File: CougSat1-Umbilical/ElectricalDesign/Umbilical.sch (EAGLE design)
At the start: 5 parts, among them J2 HR10A-10P-10P, J3 EJ501C

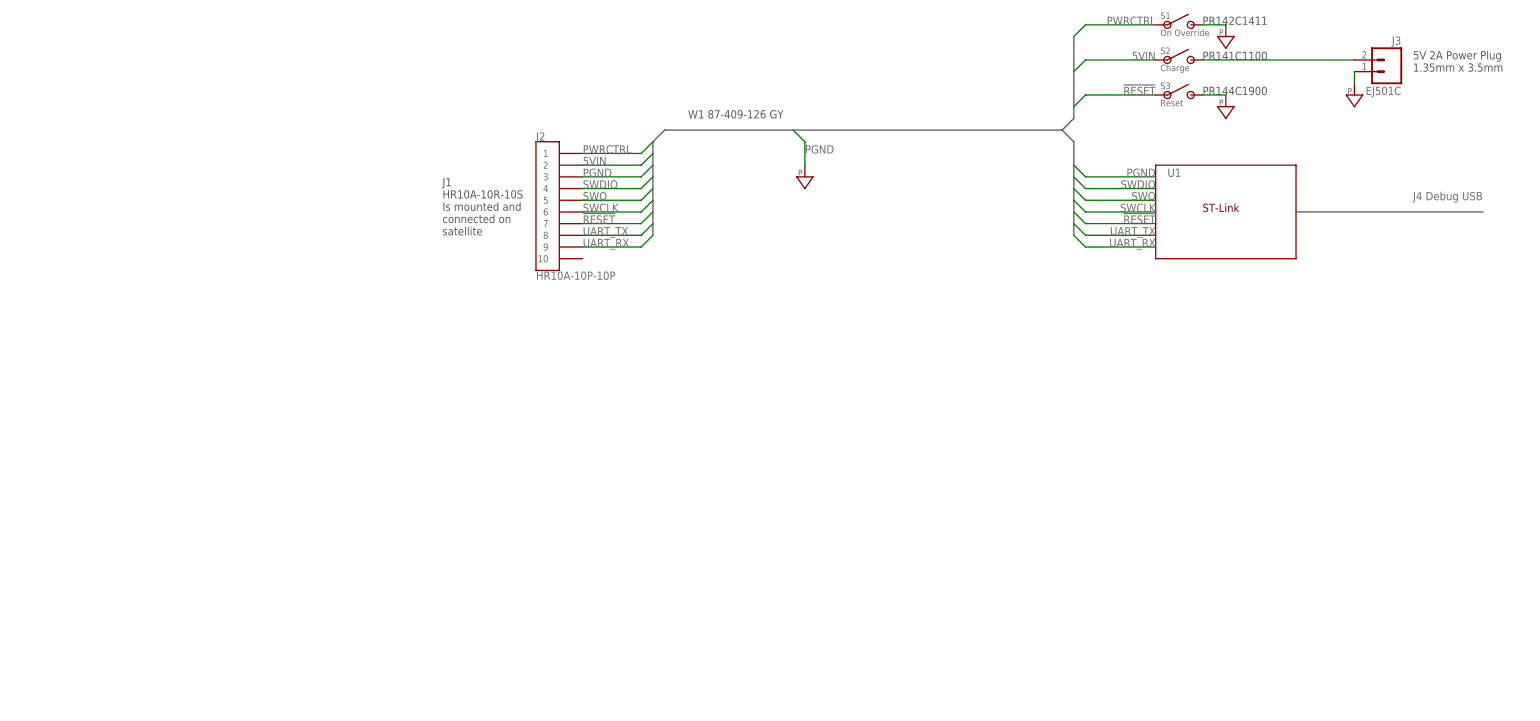
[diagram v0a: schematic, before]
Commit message: Created Umbilical Block Diagram
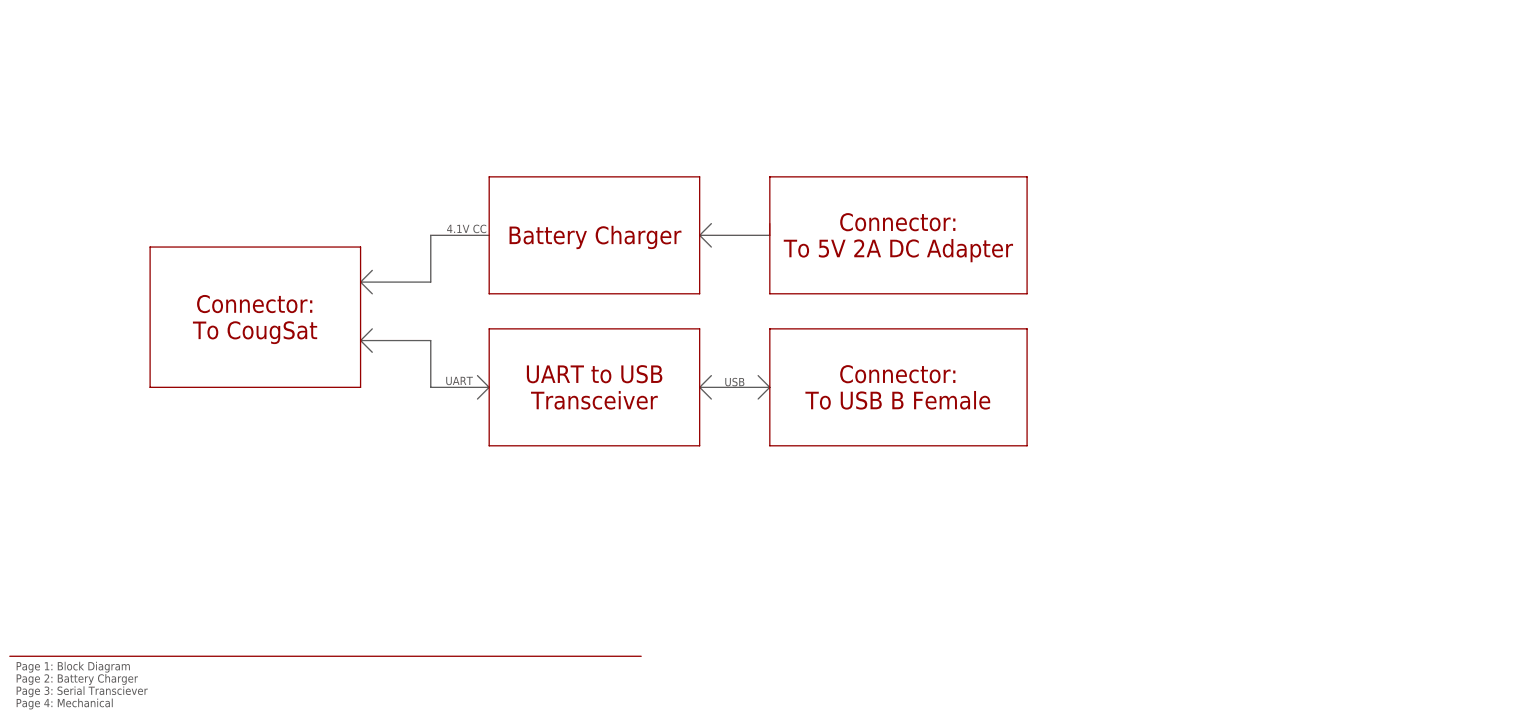
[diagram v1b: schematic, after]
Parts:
- removed J2: HR10A-10P-10P, CougsInSpace:CONN_101X10_SMD-2.5MM
- removed J3: EJ501C, CougsInSpace:CONN_021X02_SMD-2.5MM
- removed S1: On Override, CougsInSpace:TACTILE_SWITCH6.2MMX6.2MM
- removed S2: Charge, CougsInSpace:TACTILE_SWITCH6.2MMX6.2MM
- removed S3: Reset, CougsInSpace:TACTILE_SWITCH6.2MMX6.2MM
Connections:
- removed net !RESET: J2.7, S3.1
- removed net 5VIN: J2.2, S2.1
- removed net N$1: J3.2, S2.2
- removed net PGND: J2.3, J3.1, S1.2, S3.2
- removed net PWRCTRL: J2.1, S1.1
- removed net SWCLK: J2.6
- removed net SWDIO: J2.4
- removed net SWO: J2.5
- removed net UART_RX: J2.9
- removed net UART_TX: J2.8
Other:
- note added: "4.1V CC"
- note added: "Battery Charger"
- note added: "Connector: To 5V 2A DC Adapter"
- note added: "Connector: To CougSat"
- note added: "Connector: To USB B Female"
- note added: "Page 1: Block Diagram Page 2: Battery Charger Page 3: Serial Transciever Page 4: Mechanical"
- note added: "UART"
- note added: "UART to USB Transceiver"
- note added: "USB"
- note removed: "5V 2A Power Plug 1.35mm x 3.5mm"
- note removed: "J1 HR10A-10R-10S Is mounted and connected on satellite"
- note removed: "J4 Debug USB"
- note removed: "PR141C1100"
- note removed: "PR142C1411"
- note removed: "PR144C1900"
- note removed: "ST-Link"
- note removed: "U1"
- note removed: "W1 87-409-126 GY"

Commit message: Update CougSat1-Umbilical/ElectricalDesign/Umbilical.sch
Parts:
- added C1, C10, C12, C4: 100nF 10%, CougsInSpace-Capacitors:CAP-V-100NF-1608
- added C11, C7, C8: 1µF 10%, CougsInSpace-Capacitors:CAP-V-1UF-1608
- added C13, C9: 10µF 10%, CougsInSpace-Capacitors:CAP-V-10UF-1608
- added C14: 4.7µF 10%, CougsInSpace-Capacitors:CAP-V-4.7UF-3216
- added C15: 22pF 5%, CougsInSpace-Capacitors:CAP-V-22PF-1608
- added C2, C3: 47pF 5%, CougsInSpace-Capacitors:CAP-V-47PF-1608
- added C5: 10nF 10%, CougsInSpace-Capacitors:CAP-V-10NF-1608
- added C6: 4.7pF ±0.1, CougsInSpace-Capacitors:CAP-V-4.7PF-1608
- added D1: LTC4411, CougsInSpace-DiscreteSemi:LTC4411
- added D2: MBRM120LT, CougsInSpace-DiscreteSemi:DIODE-SCHOTTKY-H-POWERMITE
- added DS1: Green, CougsInSpace-LEDs:LED-H-GRN-1608
- added DS2: Red, CougsInSpace-LEDs:LED-H-RED-1608
- added FB1: 1.5kΩ @ 100MHz, CougsInSpace-Coils:CHOKE-H-1.5K-1608
- added J1: (no value), CougsInSpace-Connectors:USB-B-FEMALE
- added J2: (no value), CougsInSpace-Connectors:1X04-PICOLOCK
- added J3: (no value), CougsInSpace-Connectors:BARREL-2.1X5.5-R
- added L1: 10µH 20%, CougsInSpace-Coils:INDUCTOR-H-10UH-6060
- added Q1, Q2: CSD16406Q3, CougsInSpace-DiscreteSemi:MOSFET-N-SON-3333
- added R1: 0Ω <20mΩ, CougsInSpace-Resistors:RES-V-0-1608
- added R10: 12.1kΩ 0.1%, CougsInSpace-Resistors:RES-V-12.1K-1608
- added R11: 2.2kΩ 1%, CougsInSpace-Resistors:RES-V-2.2K-1608
- added R12: 3.3kΩ 0.1%, CougsInSpace-Resistors:RES-V-3.3K-1608
- added R2, R3: 27Ω 1%, CougsInSpace-Resistors:RES-H-27R-1608
- added R4: 10Ω 5%, CougsInSpace-Resistors:RES-H-10R-TO220
- added R5, R6: 10kΩ 0.1%, CougsInSpace-Resistors:RES-H-10K-1608
- added R7: 10mΩ 1%, CougsInSpace-Resistors:RES-H-0.01R-3216
- added R8: 10mΩ 1%, CougsInSpace-Resistors:RES-V-0.01R-3216
- added R9: 10kΩ 0.1%, CougsInSpace-Resistors:RES-V-10K-1608
- added U1: FT230XQ, CougsInSpace-IC-Conversion:FT230X-QFN16
- added U2: BQ24650, CougsInSpace-IC-Power:BQ24650
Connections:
- new net 3.3V: C1.1, U1.!RESET, U1.3V3OUT, U1.VCCIO
- new net 5.0V: D1.IN, J3.CENTER, R5.1, R6.1, U2.MPPSET
- new net DGND: C1.2, R1.1, U1.DGND
- new net N$1: C11.1, D2.A, U2.REGN
- new net N$10: C8.1, R11.2, U2.VREF
- new net N$11: C10.2, L1.1, Q1.D, Q2.S, U2.PH
- new net N$12: Q2.G, U2.HIGHDV
- new net N$13: Q1.G, U2.LODRV
- new net N$14: R7.2, R8.2
- new net N$15: C12.1, L1.2, R7.1, U2.SR_P
- new net N$16: C12.2, C13.1, C14.1, C15.1, R8.1, R9.2, U2.SR_N
- new net N$18: C15.2, R10.2, R9.1, U2.VFB
- new net N$19: R11.1, R12.2, U2.TS
- new net N$2: C9.1, D1.OUT, Q2.D, R4.1
- new net N$3: U2.THERM_EN
- new net N$4: C10.1, D2.C, U2.BTST
- new net N$5: DS1.C, U2.STAT2
- new net N$6: C7.1, R4.2, U2.VCC
- new net N$7: DS1.A, R5.2
- new net N$8: DS2.A, R6.2
- new net N$9: DS2.C, U2.STAT1
- new net PGND: C11.2, C13.2, C14.2, C2.2, C3.2, C4.2, C5.2, C6.2, C7.2, C8.2, C9.2, D1.CTL, D1.GND, D1.STAT, J1.GND, J1.SHIELD, J2.4, J3.SLEEVE, J3.SW, Q1.S, R1.2, R10.1, R12.1, U2.PAD, U2.PGND
- new net UMB_IN: J2.1
- new net UMB_RX: J2.2, U1.TXD
- new net UMB_TX: J2.3, U1.RXD
- new net USB5V: C5.1, FB1.1, J1.VCC
- new net USB5V_FILTERED: C4.1, C6.1, FB1.2, U1.VCC
- new net USB_CONN_N: C2.1, J1.DATA_N, R3.1
- new net USB_CONN_P: C3.1, J1.DATA_P, R2.1
- new net USB_N: R3.2, U1.USBD_N
- new net USB_P: R2.2, U1.USBD_P
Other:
- note added: "2xx>"
- note added: "3XX>"
- note added: "CAD Note: Decoupling"

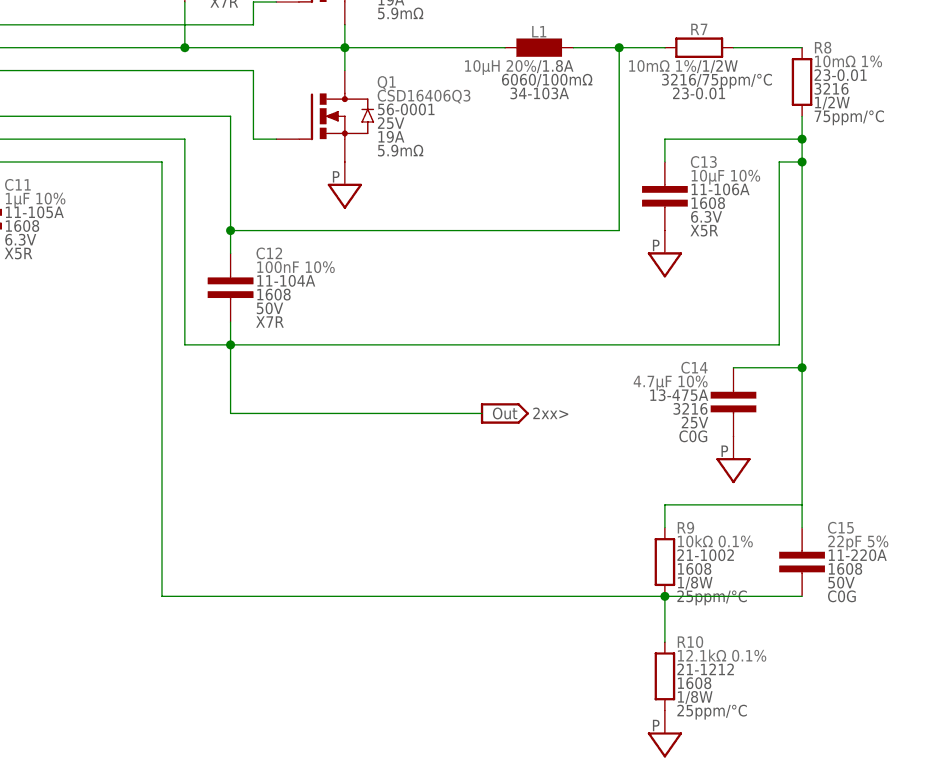
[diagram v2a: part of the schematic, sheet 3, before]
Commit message: Update CougSat1-Umbilical/ElectricalDesign/Umbilical.sch
Finished Umbilical schematic
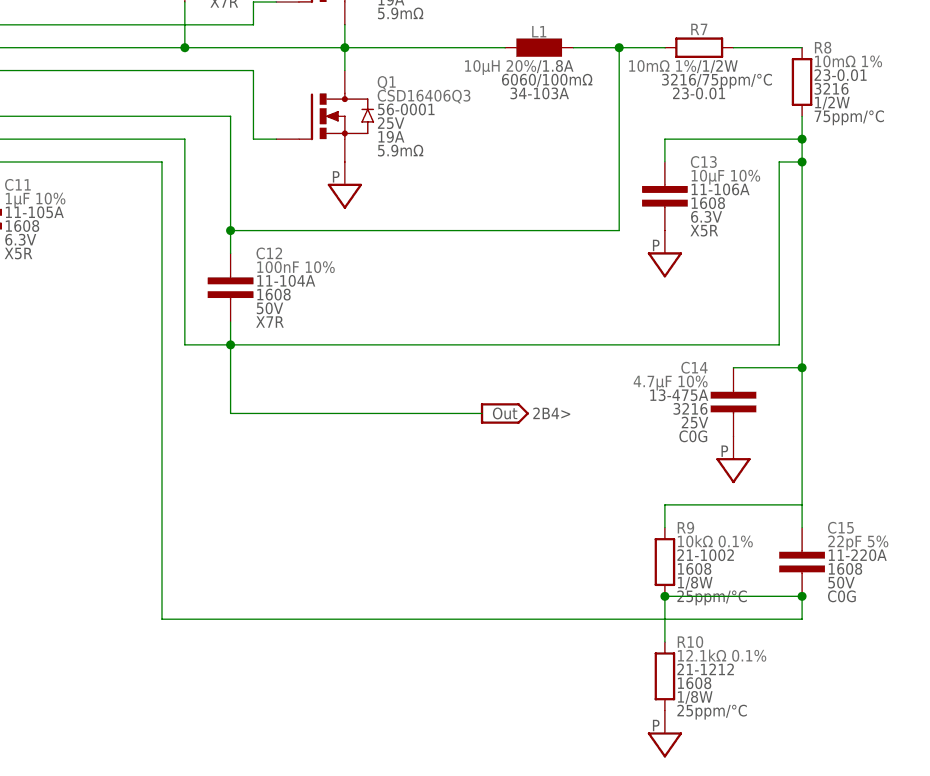
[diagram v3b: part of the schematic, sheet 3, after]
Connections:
- net N$1 renamed REGN
- net N$10 renamed VREF
- net N$11 renamed PH
- net N$12 renamed HIGHDV
- net N$13 renamed LODRV
- net N$15 renamed SR_P
- net N$16 renamed BAT_CHARGE_OUT
- net N$18 renamed VFB
- net N$19 renamed TS
- net N$2 renamed DIODE_OUT
- net N$4 renamed BTST
- net N$5 renamed CHARGING_STAT_G
- net N$6 renamed VCC
- net N$9 renamed CHARGING_STAT_R
- new net BARREL_MPPSET: D1.IN, J3.CENTER, U2.MPPSET
- net 5.0V: no longer D1.IN, J3.CENTER, U2.MPPSET
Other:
- note added: "2B4>"
- note added: "3C5>"
- note added: "Page 2"
- note added: "Page 3"
- note removed: "2xx>"
- note removed: "3XX>"
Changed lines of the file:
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@@
 <attribute name="TITLE" value="Block Diagram"/>
 </part>
-<part name="FRAME2" library="CougsInSpace-Aesthetics" deviceset="FRAME-A" device=""/>
+<part name="FRAME2" library="CougsInSpace-Aesthetics" deviceset="FRAME-A" device="">
+<attribute name="TITLE" value="Serial Transeiver"/>
+</part>
 <part name="U1" library="CougsInSpace-IC-Conversion" deviceset="FT230X" device="-QFN16" value="FT230XQ"/>
 <part name="J1" library="CougsInSpace-Connectors" deviceset="USB" device="-B-FEMALE"/>
@@
 <part name="C5" library="CougsInSpace-Capacitors" deviceset="CAP-V" device="-1608" technology="-10NF" value="10nF 10%"/>
 <part name="C6" library="CougsInSpace-Capacitors" deviceset="CAP-V" device="-1608" technology="-4.7PF" value="4.7pF ±0.1"/>
-<part name="FRAME3" library="CougsInSpace-Aesthetics" deviceset="FRAME-A" device=""/>
+<part name="FRAME3" library="CougsInSpace-Aesthetics" deviceset="FRAME-A" device="">
+<attribute name="TITLE" value="Battery Charger"/>
+</part>
 <part name="U2" library="CougsInSpace-IC-Power" deviceset="BQ24650" device="" value="BQ24650"/>
 <part name="C7" library="CougsInSpace-Capacitors" deviceset="CAP-V" device="-1608" technology="-1UF" value="1µF 10%"/>
@@
 <text x="100.584" y="84.328" size="1.778" layer="97" align="bottom-right">UART</text>
 <text x="157.48" y="84.074" size="1.778" layer="97" align="bottom-center">USB</text>
+<text x="147.32" y="73.66" size="1.27" layer="97" rot="R180" align="center-left">Page 2</text>
+<text x="147.32" y="106.68" size="1.27" layer="97" rot="R180" align="center-left">Page 3</text>
 </plain>
 <instances>
@@
 <wire x1="101.6" y1="101.6" x2="132.08" y2="101.6" width="0.1524" layer="97" style="shortdash"/>
 <text x="104.14" y="76.2" size="1.778" layer="97">CAD Note: Decoupling</text>
-<text x="137.16" y="134.62" size="1.27" layer="97" align="center-right">3XX&gt; </text>
+<text x="137.16" y="134.62" size="1.27" layer="97" align="center-right">3C5&gt; </text>
 </plain>
 <instances>
@@
 <attribute name="REV" x="257.81" y="7.62" size="3.81" layer="94" ratio="15" align="bottom-right"/>
 <attribute name="SHEET" x="257.81" y="1.27" size="3.81" layer="94" ratio="15" align="bottom-right"/>
+<attribute name="TITLE" x="227.33" y="20.32" size="3.81" layer="94" ratio="15" align="bottom-right"/>
 </instance>
 <instance part="U1" gate="G$1" x="116.84" y="121.92" smashed="yes">
@@
 <sheet>
 <plain>
-<text x="215.9" y="68.58" size="1.27" layer="97" align="center-left"> 2xx&gt;</text>
+<text x="215.9" y="68.58" size="1.27" layer="97" align="center-left"> 2B4&gt;</text>
 </plain>
 <instances>
@@
 <attribute name="REV" x="257.81" y="7.62" size="3.81" layer="94" ratio="15" align="bottom-right"/>
 <attribute name="SHEET" x="257.81" y="1.27" size="3.81" layer="94" ratio="15" align="bottom-right"/>
+<attribute name="TITLE" x="227.33" y="20.32" size="3.81" layer="94" ratio="15" align="bottom-right"/>
 </instance>
 <instance part="U2" gate="G$1" x="132.08" y="111.76" smashed="yes">
@@
 </segment>
 </net>
-<net name="N$2" class="0">
+<net name="DIODE_OUT" class="0">
 <segment>
 <pinref part="R4" gate="G$1" pin="1"/>
@@
 </segment>
 </net>
-<net name="N$4" class="0">
+<net name="BTST" class="0">
 <segment>
 <pinref part="U2" gate="G$1" pin="BTST"/>
@@
 <net name="5.0V" class="0">
 <segment>
-<pinref part="J3" gate="G$1" pin="CENTER"/>
-<pinref part="D1" gate="G$1" pin="IN"/>
-<wire x1="35.56" y1="165.1" x2="38.1" y2="165.1" width="0.1524" layer="91"/>
-<wire x1="38.1" y1="165.1" x2="78.74" y2="165.1" width="0.1524" layer="91"/>
-<pinref part="SUPPLY4" gate="G$1" pin="5.0V"/>
-<wire x1="78.74" y1="165.1" x2="86.36" y2="165.1" width="0.1524" layer="91"/>
-<wire x1="38.1" y1="167.64" x2="38.1" y2="165.1" width="0.1524" layer="91"/>
-<junction x="38.1" y="165.1"/>
-<pinref part="U2" gate="G$1" pin="MPPSET"/>
-<wire x1="116.84" y1="119.38" x2="78.74" y2="119.38" width="0.1524" layer="91"/>
-<wire x1="78.74" y1="119.38" x2="78.74" y2="165.1" width="0.1524" layer="91"/>
-<junction x="78.74" y="165.1"/>
-</segment>
-<segment>
 <pinref part="R5" gate="G$1" pin="1"/>
 <wire x1="55.88" y1="76.2" x2="48.26" y2="76.2" width="0.1524" layer="91"/>
@@
 </segment>
 </net>
-<net name="N$5" class="0">
+<net name="CHARGING_STAT_G" class="0">
 <segment>
 <pinref part="DS1" gate="G$1" pin="C"/>
@@
 </segment>
 </net>
-<net name="N$10" class="0">
+<net name="VREF" class="0">
 <segment>
 <wire x1="106.68" y1="127" x2="106.68" y2="68.58" width="0.1524" layer="91"/>
@@
 </segment>
 </net>
-<net name="N$9" class="0">
+<net name="CHARGING_STAT_R" class="0">
 <segment>
 <pinref part="U2" gate="G$1" pin="STAT1"/>
@@
 </segment>
 </net>
-<net name="N$6" class="0">
+<net name="VCC" class="0">
 <segment>
 <pinref part="U2" gate="G$1" pin="VCC"/>
@@
 </segment>
 </net>
-<net name="N$11" class="0">
+<net name="PH" class="0">
 <segment>
 <pinref part="Q2" gate="G$1" pin="S"/>
@@
 </segment>
 </net>
-<net name="N$12" class="0">
+<net name="HIGHDV" class="0">
 <segment>
 <pinref part="U2" gate="G$1" pin="HIGHDV"/>
@@
 </segment>
 </net>
-<net name="N$13" class="0">
+<net name="LODRV" class="0">
 <segment>
 <pinref part="U2" gate="G$1" pin="LODRV"/>
@@
 </segment>
 </net>
-<net name="N$1" class="0">
+<net name="REGN" class="0">
 <segment>
 <pinref part="U2" gate="G$1" pin="REGN"/>
@@
 </segment>
 </net>
-<net name="N$15" class="0">
+<net name="SR_P" class="0">
 <segment>
 <pinref part="U2" gate="G$1" pin="SR_P"/>
@@
 </segment>
 </net>
-<net name="N$16" class="0">
+<net name="BAT_CHARGE_OUT" class="0">
 <segment>
 <pinref part="U2" gate="G$1" pin="SR_N"/>
@@
 </segment>
 </net>
-<net name="N$18" class="0">
+<net name="VFB" class="0">
 <segment>
 <pinref part="U2" gate="G$1" pin="VFB"/>
@@
 <pinref part="C15" gate="G$1" pin="2"/>
 <wire x1="246.38" y1="48.26" x2="231.14" y2="48.26" width="0.1524" layer="91"/>
-<wire x1="231.14" y1="48.26" x2="175.26" y2="48.26" width="0.1524" layer="91"/>
-<wire x1="175.26" y1="48.26" x2="175.26" y2="96.52" width="0.1524" layer="91"/>
+<wire x1="175.26" y1="45.72" x2="175.26" y2="96.52" width="0.1524" layer="91"/>
 <pinref part="R10" gate="G$1" pin="2"/>
 <wire x1="231.14" y1="43.18" x2="231.14" y2="48.26" width="0.1524" layer="91"/>
 <junction x="231.14" y="48.26"/>
 <pinref part="R9" gate="G$1" pin="1"/>
-</segment>
-</net>
-<net name="N$19" class="0">
+<wire x1="175.26" y1="45.72" x2="246.38" y2="45.72" width="0.1524" layer="91"/>
+<wire x1="246.38" y1="45.72" x2="246.38" y2="48.26" width="0.1524" layer="91"/>
+<junction x="246.38" y="48.26"/>
+</segment>
+</net>
+<net name="TS" class="0">
 <segment>
 <pinref part="R11" gate="G$1" pin="1"/>
@@
 </segment>
 </net>
+<net name="BARREL_MPPSET" class="0">
+<segment>
+<pinref part="J3" gate="G$1" pin="CENTER"/>
+<pinref part="D1" gate="G$1" pin="IN"/>
+<wire x1="35.56" y1="165.1" x2="38.1" y2="165.1" width="0.1524" layer="91"/>
+<wire x1="38.1" y1="165.1" x2="78.74" y2="165.1" width="0.1524" layer="91"/>
+<pinref part="SUPPLY4" gate="G$1" pin="5.0V"/>
+<wire x1="78.74" y1="165.1" x2="86.36" y2="165.1" width="0.1524" layer="91"/>
+<wire x1="38.1" y1="167.64" x2="38.1" y2="165.1" width="0.1524" layer="91"/>
+<junction x="38.1" y="165.1"/>
+<pinref part="U2" gate="G$1" pin="MPPSET"/>
+<wire x1="116.84" y1="119.38" x2="78.74" y2="119.38" width="0.1524" layer="91"/>
+<wire x1="78.74" y1="119.38" x2="78.74" y2="165.1" width="0.1524" layer="91"/>
+<junction x="78.74" y="165.1"/>
+</segment>
+</net>
